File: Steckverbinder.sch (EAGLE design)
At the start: 1 part, among them X1 MAC64L

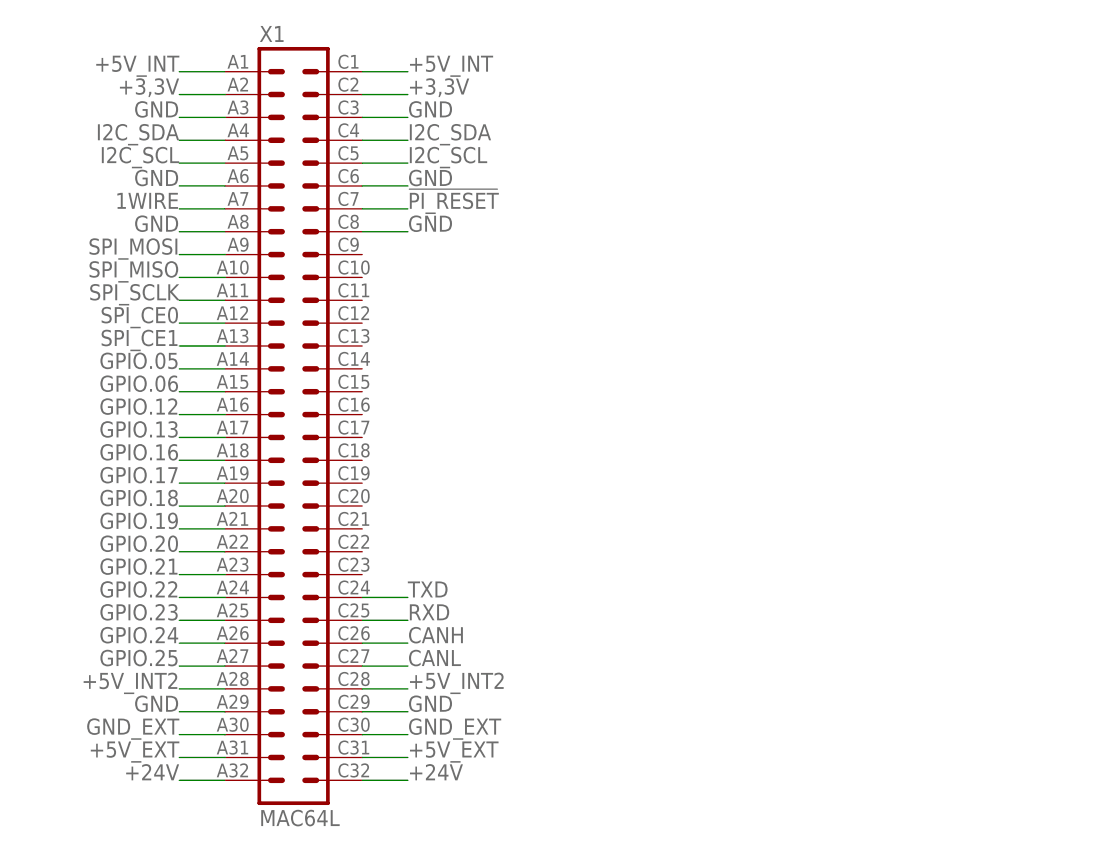
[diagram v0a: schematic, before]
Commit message: Pi, CanBus, Stromversorgung, Steckverbinder angepasst
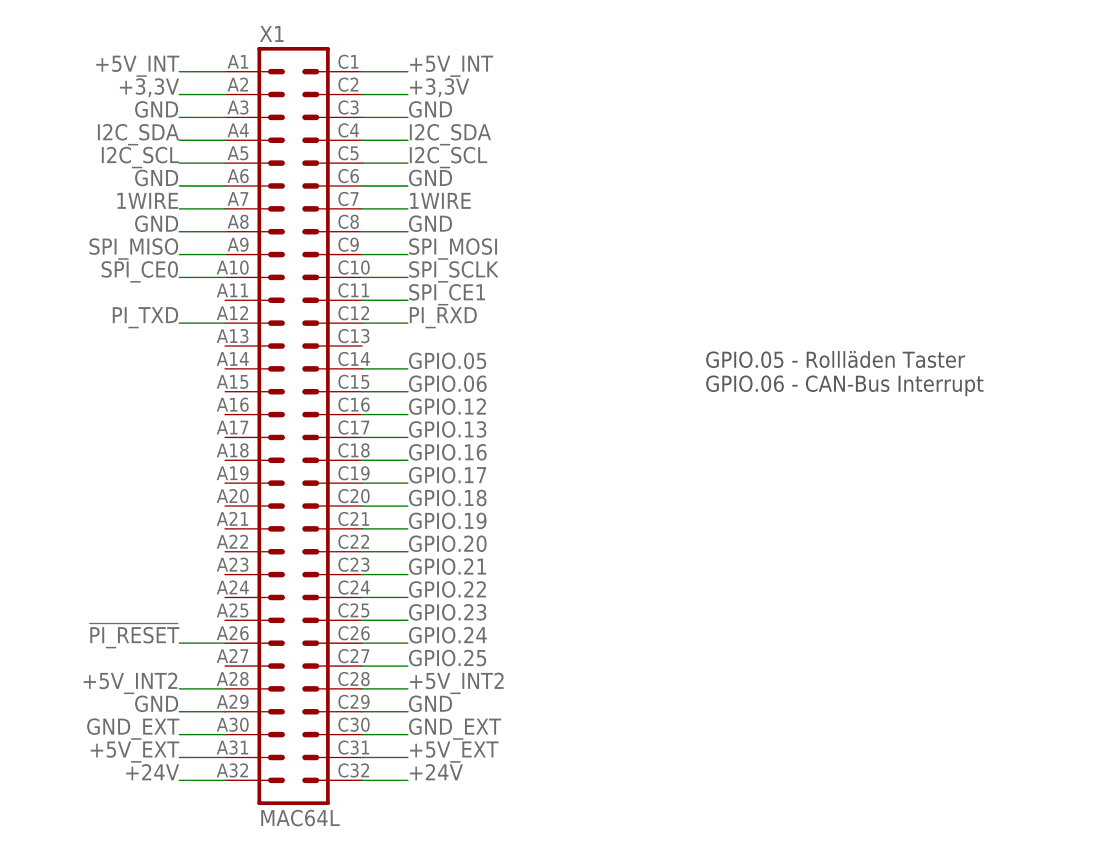
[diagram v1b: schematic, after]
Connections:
- removed net CANH: X1.C26
- removed net CANL: X1.C27
- removed net RXD: X1.C25
- removed net TXD: X1.C24
- new net PI_RXD: X1.C12
- new net PI_TXD: X1.A12
- net !PI_RESET: now also X1.A26; no longer X1.C7
- net 1WIRE: now also X1.C7
- net GPIO.05: now also X1.C14; no longer X1.A14
- net GPIO.06: now also X1.C15; no longer X1.A15
- net GPIO.12: now also X1.C16; no longer X1.A16
- net GPIO.13: now also X1.C17; no longer X1.A17
- net GPIO.16: now also X1.C18; no longer X1.A18
- net GPIO.17: now also X1.C19; no longer X1.A19
- net GPIO.18: now also X1.C20; no longer X1.A20
- net GPIO.19: now also X1.C21; no longer X1.A21
- net GPIO.20: now also X1.C22; no longer X1.A22
- net GPIO.21: now also X1.C23; no longer X1.A23
- net GPIO.22: now also X1.C24; no longer X1.A24
- net GPIO.23: now also X1.C25; no longer X1.A25
- net GPIO.24: now also X1.C26; no longer X1.A26
- net GPIO.25: now also X1.C27; no longer X1.A27
- net SPI_CE0: now also X1.A10; no longer X1.A12
- net SPI_CE1: now also X1.C11; no longer X1.A13
- net SPI_MISO: now also X1.A9; no longer X1.A10
- net SPI_MOSI: now also X1.C9; no longer X1.A9
- net SPI_SCLK: now also X1.C10; no longer X1.A11
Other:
- note added: "GPIO.05 - Rollläden Taster GPIO.06 - CAN-Bus Interrupt"

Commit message: Pi-Display hinzugefügt, Boards angepasst
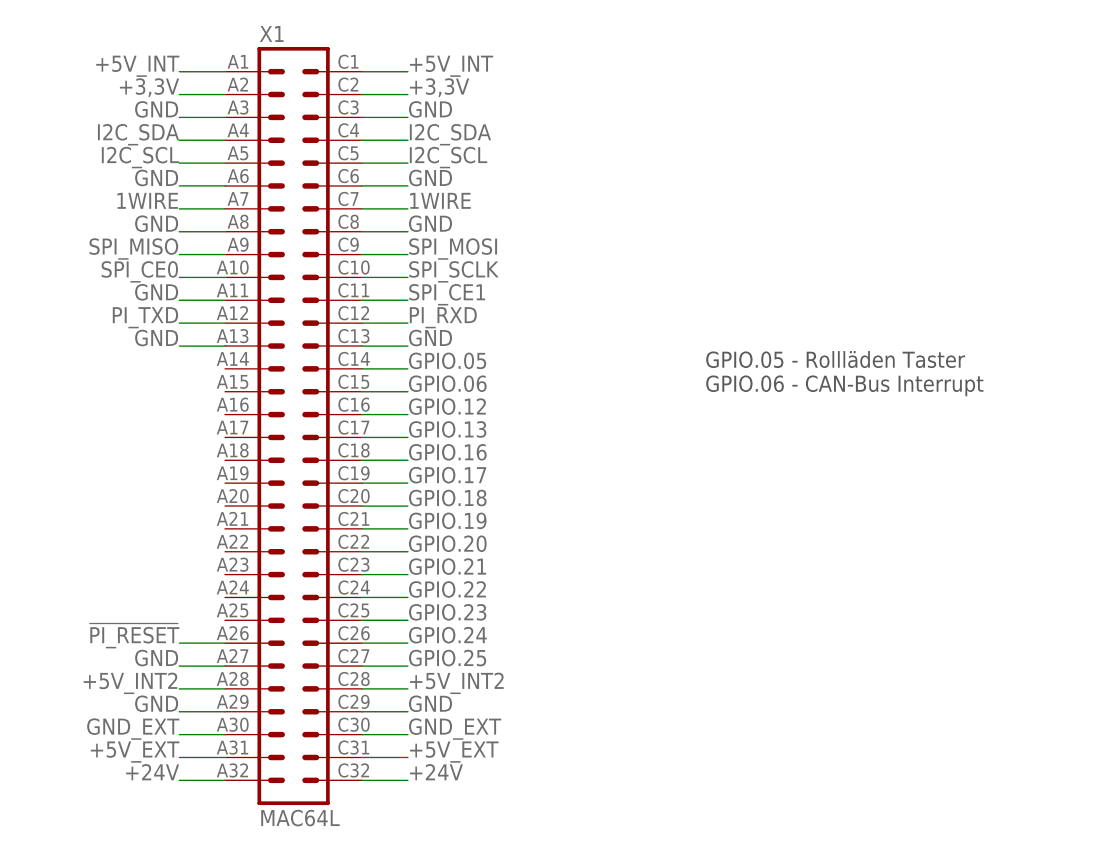
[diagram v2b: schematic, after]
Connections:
- net GND: now also X1.A11, X1.A13, X1.A27, X1.C13
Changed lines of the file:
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@@
 <label x="55.88" y="20.32" size="1.778" layer="95"/>
+</segment>
+<segment>
+<pinref part="X1" gate="G$1" pin="A11"/>
+<wire x1="35.56" y1="66.04" x2="30.48" y2="66.04" width="0.1524" layer="91"/>
+<label x="30.48" y="66.04" size="1.778" layer="95" rot="MR0"/>
+</segment>
+<segment>
+<pinref part="X1" gate="G$1" pin="A13"/>
+<wire x1="35.56" y1="60.96" x2="30.48" y2="60.96" width="0.1524" layer="91"/>
+<label x="30.48" y="60.96" size="1.778" layer="95" rot="MR0"/>
+</segment>
+<segment>
+<pinref part="X1" gate="G$1" pin="C13"/>
+<wire x1="50.8" y1="60.96" x2="55.88" y2="60.96" width="0.1524" layer="91"/>
+<label x="55.88" y="60.96" size="1.778" layer="95"/>
+</segment>
+<segment>
+<pinref part="X1" gate="G$1" pin="A27"/>
+<wire x1="35.56" y1="25.4" x2="30.48" y2="25.4" width="0.1524" layer="91"/>
+<label x="30.48" y="25.4" size="1.778" layer="95" rot="MR0"/>
 </segment>
 </net>

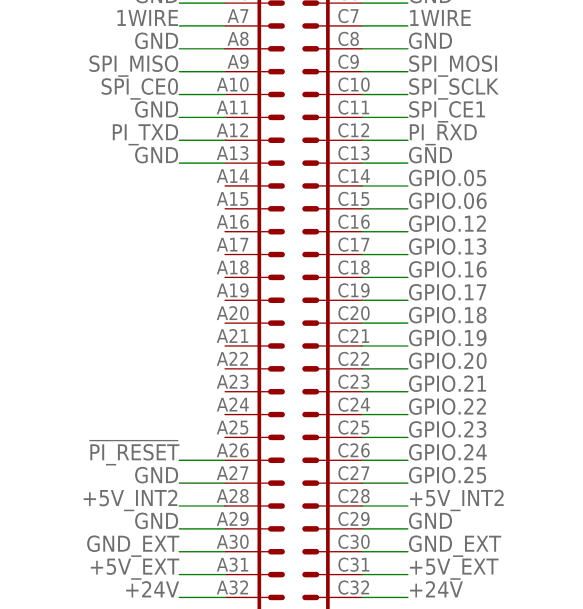
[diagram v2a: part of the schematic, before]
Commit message: Schaltpläne aufgehübscht zur Veröffentlichung
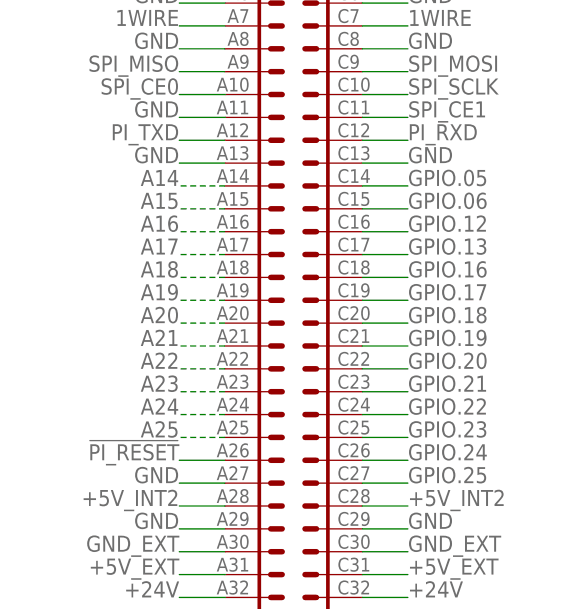
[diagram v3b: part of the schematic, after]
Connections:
- new net A14: X1.A14
- new net A15: X1.A15
- new net A16: X1.A16
- new net A17: X1.A17
- new net A18: X1.A18
- new net A19: X1.A19
- new net A20: X1.A20
- new net A21: X1.A21
- new net A22: X1.A22
- new net A23: X1.A23
- new net A24: X1.A24
- new net A25: X1.A25
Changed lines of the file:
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@@
+</segment>
+</net>
+<net name="A14" class="0">
+<segment>
+<pinref part="X1" gate="G$1" pin="A14"/>
+<wire x1="35.56" y1="58.42" x2="30.48" y2="58.42" width="0.1524" layer="91" style="longdash"/>
+<label x="30.48" y="58.42" size="1.778" layer="95" rot="MR0"/>
+</segment>
+</net>
+<net name="A15" class="0">
+<segment>
+<pinref part="X1" gate="G$1" pin="A15"/>
+<wire x1="35.56" y1="55.88" x2="30.48" y2="55.88" width="0.1524" layer="91" style="longdash"/>
+<label x="30.48" y="55.88" size="1.778" layer="95" rot="MR0"/>
+</segment>
+</net>
+<net name="A16" class="0">
+<segment>
+<pinref part="X1" gate="G$1" pin="A16"/>
+<wire x1="35.56" y1="53.34" x2="30.48" y2="53.34" width="0.1524" layer="91" style="longdash"/>
+<label x="30.48" y="53.34" size="1.778" layer="95" rot="MR0"/>
+</segment>
+</net>
+<net name="A17" class="0">
+<segment>
+<pinref part="X1" gate="G$1" pin="A17"/>
+<wire x1="35.56" y1="50.8" x2="30.48" y2="50.8" width="0.1524" layer="91" style="longdash"/>
+<label x="30.48" y="50.8" size="1.778" layer="95" rot="MR0"/>
+</segment>
+</net>
+<net name="A18" class="0">
+<segment>
+<pinref part="X1" gate="G$1" pin="A18"/>
+<wire x1="35.56" y1="48.26" x2="30.48" y2="48.26" width="0.1524" layer="91" style="longdash"/>
+<label x="30.48" y="48.26" size="1.778" layer="95" rot="MR0"/>
+</segment>
+</net>
+<net name="A19" class="0">
+<segment>
+<pinref part="X1" gate="G$1" pin="A19"/>
+<wire x1="35.56" y1="45.72" x2="30.48" y2="45.72" width="0.1524" layer="91" style="longdash"/>
+<label x="30.48" y="45.72" size="1.778" layer="95" rot="MR0"/>
+</segment>
+</net>
+<net name="A20" class="0">
+<segment>
+<pinref part="X1" gate="G$1" pin="A20"/>
+<wire x1="35.56" y1="43.18" x2="30.48" y2="43.18" width="0.1524" layer="91" style="longdash"/>
+<label x="30.48" y="43.18" size="1.778" layer="95" rot="MR0"/>
+</segment>
+</net>
+<net name="A21" class="0">
+<segment>
+<pinref part="X1" gate="G$1" pin="A21"/>
+<wire x1="35.56" y1="40.64" x2="30.48" y2="40.64" width="0.1524" layer="91" style="longdash"/>
+<label x="30.48" y="40.64" size="1.778" layer="95" rot="MR0"/>
+</segment>
+</net>
+<net name="A22" class="0">
+<segment>
+<pinref part="X1" gate="G$1" pin="A22"/>
+<wire x1="35.56" y1="38.1" x2="30.48" y2="38.1" width="0.1524" layer="91" style="longdash"/>
+<label x="30.48" y="38.1" size="1.778" layer="95" rot="MR0"/>
+</segment>
+</net>
+<net name="A23" class="0">
+<segment>
+<pinref part="X1" gate="G$1" pin="A23"/>
+<wire x1="35.56" y1="35.56" x2="30.48" y2="35.56" width="0.1524" layer="91" style="longdash"/>
+<label x="30.48" y="35.56" size="1.778" layer="95" rot="MR0"/>
+</segment>
+</net>
+<net name="A24" class="0">
+<segment>
+<pinref part="X1" gate="G$1" pin="A24"/>
+<wire x1="35.56" y1="33.02" x2="30.48" y2="33.02" width="0.1524" layer="91" style="longdash"/>
+<label x="30.48" y="33.02" size="1.778" layer="95" rot="MR0"/>
+</segment>
+</net>
+<net name="A25" class="0">
+<segment>
+<pinref part="X1" gate="G$1" pin="A25"/>
+<wire x1="35.56" y1="30.48" x2="30.48" y2="30.48" width="0.1524" layer="91" style="longdash"/>
+<label x="30.48" y="30.48" size="1.778" layer="95" rot="MR0"/>
 </segment>
 </net>

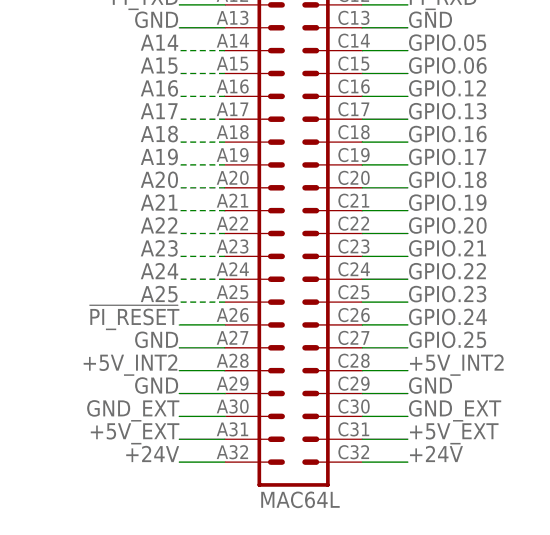
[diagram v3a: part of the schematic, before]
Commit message: Verbesserte Stromversorgung, Pi-Kühler, CAN-Bus 8x-Schalter
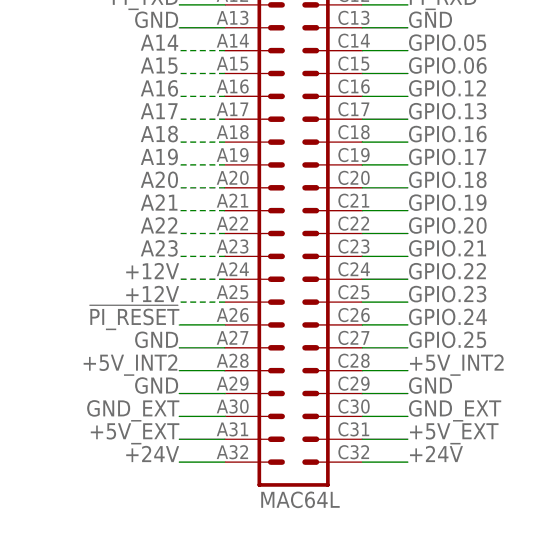
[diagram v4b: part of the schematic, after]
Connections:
- removed net A24: X1.A24
- removed net A25: X1.A25
- new net +12V: X1.A24, X1.A25
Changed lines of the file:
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@@
 </segment>
 </net>
-<net name="A24" class="0">
+<net name="+12V" class="0">
 <segment>
 <pinref part="X1" gate="G$1" pin="A24"/>
@@
 <label x="30.48" y="33.02" size="1.778" layer="95" rot="MR0"/>
 </segment>
-</net>
-<net name="A25" class="0">
 <segment>
 <pinref part="X1" gate="G$1" pin="A25"/>
